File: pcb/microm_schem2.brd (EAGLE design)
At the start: 101.6 x 81.3 mm, 77 parts, among them Q1 16 MHz

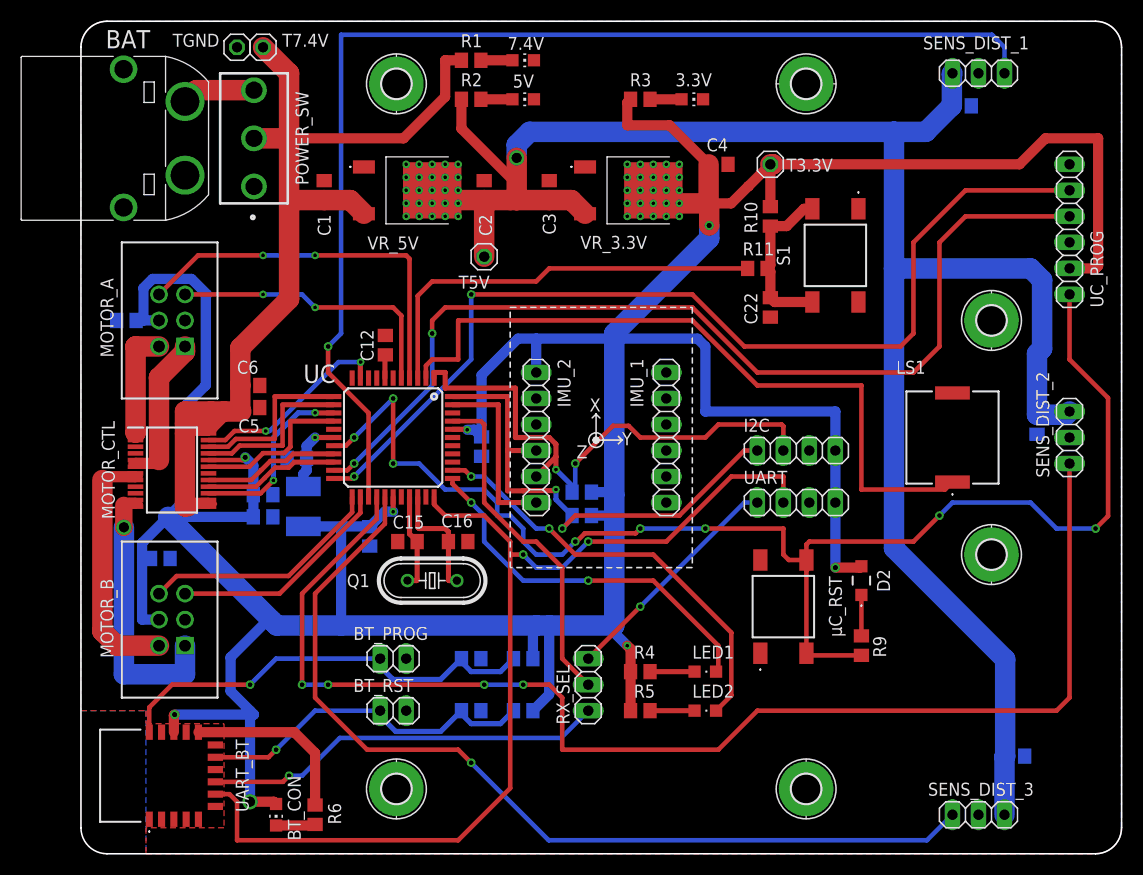
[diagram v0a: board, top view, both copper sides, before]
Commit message: Optimizations on pcb, unify via sizes and trace widths.
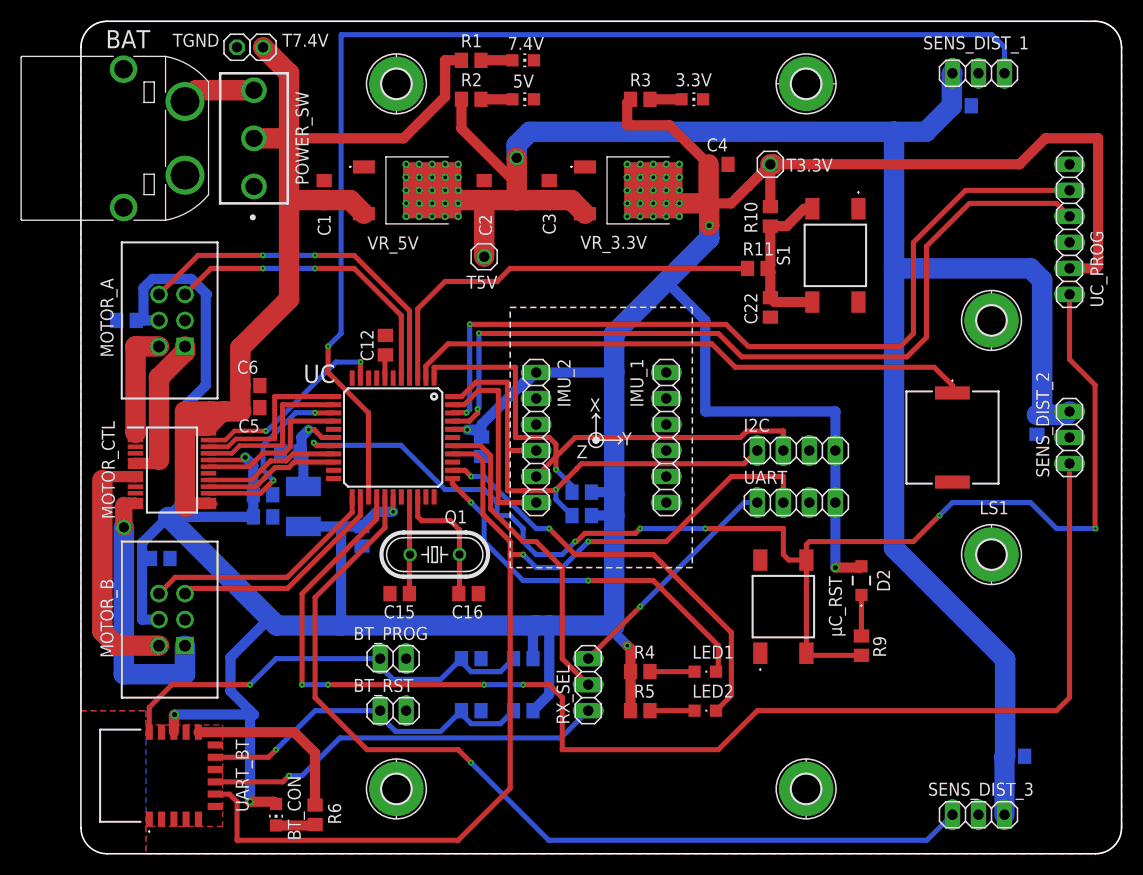
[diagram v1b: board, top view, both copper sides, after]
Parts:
- moved C16 5.18 mm to (37.8, 25.4)
- moved C15 5.14 mm to (31.1, 25.4)
- moved Q1 2.55 mm to (34.5, 29.2)
- moved C11 0.90 mm to (20.4, 39.2)
- moved C10 0.76 mm to (27.4, 31.0)
- turned LS1 to 270 degrees
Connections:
- removed net PG_EC1: UC.22, UC_PROG.5
- removed net PG_ED1: UC.21, UC_PROG.4
- new net PG_EC3: UC.42, UC_PROG.5
- new net PG_ED3: UC.41, UC_PROG.4
- net UART_RX: now also UC.38; no longer UC.41
- net UART_TX: now also UC.37; no longer UC.33
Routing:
- net PG_ED1: track 97.0 -> 0.00 mm, vias 2 -> 0
- net PG_EC1: track 96.6 -> 0.00 mm, vias 2 -> 0
- net PG_ED3: track 0.00 -> 81.1 mm, vias 0 -> 2
- net PG_EC3: track 0.00 -> 81.1 mm, vias 0 -> 2
- net BUZZ_PWM: track 69.8 -> 55.9 mm
- net +3V3: track 396.8 -> 388.0 mm
- net MCLR: track 134.7 -> 130.3 mm, vias 8 -> 6
- net MA_ENC_A: track 37.8 -> 34.8 mm
- net UART_TX: track 102.1 -> 104.7 mm
- net UART_RX: track 33.6 -> 31.2 mm
- net MA_ENC_B: track 28.1 -> 30.2 mm
- net IMU_INT: track 17.7 -> 19.7 mm
- net N$5: track 7.07 -> 8.79 mm
- net I2C_SDA: track 55.3 -> 53.8 mm, vias 2 -> 1
- net OSC2: track 11.7 -> 12.8 mm
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
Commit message: More wiring optimizations.
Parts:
- added C23: 100nF, rcl:C0805
- added LED3, LED4: red, 2mA, 2.1V, led:CHIPLED_0805
- added R14, R15: 680Ω, rcl:R0805
- C12: value 10uF, 10-20V, low-esr -> opt
- C13: value 100nF, 10-20V, low-esr -> 10uF, 10-20V, low-esr
- C15: value 20pF, low-esr, ceramic -> 100nF, 10-20V, low-esr
- C17: value 10 uF -> 20pF, low-esr, ceramic
- C20: value 1uF -> 10 uF
- C22: value 100nF -> 1uF
- moved C17 69.1 mm to (35.9, 25.4), flipped to the top
- moved C22 53.6 mm to (26.2, 18.9), flipped to the bottom, turned to 90 degrees
- moved C20 53.3 mm to (91.2, 9.53)
- moved C19 32.5 mm to (93.3, 41.9), turned to 270 degrees
- moved C18 32.0 mm to (86.0, 73.0), turned to 180 degrees
- moved C13 25.4 mm to (29.7, 49.7), flipped to the top, turned to 270 degrees
- moved C15 23.6 mm to (7.75, 28.8), flipped to the bottom
- moved C14 23.5 mm to (4.45, 52.1), turned to 0 degrees
- moved C12 15.5 mm to (20.4, 37.2), flipped to the bottom, turned to 180 degrees
- moved R13 14.9 mm to (28.3, 14.4), turned to 90 degrees
- moved R12 14.9 mm to (28.3, 18.9), turned to 90 degrees
- moved C21 12.8 mm to (26.2, 14.4), turned to 90 degrees
- moved R11 10.9 mm to (76.2, 53.3), turned to 270 degrees
- moved R10 8.98 mm to (76.2, 63.5)
- moved BT_PROG 8.89 mm to (21.6, 18.9)
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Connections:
- new net LED3: LED3.C, UC.35
- new net LED4: LED4.C, UC.36
- new net N$61: LED3.A, R14.2
- new net N$62: LED4.A, R15.2
- net +3V3: now also C15.1, R14.1, R15.1; no longer C13.1
- net +5V: now also C20.1; no longer C17.1
- net BT_PROG: now also C22.1; no longer C21.1
- net BT_RESET: now also C21.1; no longer C20.1
- net GND: now also C13.1, C23.2; no longer C13.2
- net LED1: now also UC.33; no longer UC.34
- net LED2: now also UC.34; no longer UC.35
- net MB_ENC_A: now also UC.22; no longer UC.24
- net MB_ENC_B: now also UC.21; no longer UC.23
- net N$5: now also C12.2
- net N$6: now also C23.1; no longer C22.1
- net OSC1: now also C16.1; no longer C15.1
- net OSC2: now also C17.1; no longer C16.1
- net SENS_DIST_1: now also UC.24; no longer UC.25
- net SENS_DIST_2: now also UC.25; no longer UC.26
- net SENS_DIST_3: now also UC.23; no longer UC.27
- net UART_RX: now also UC.37; no longer UC.38
- net UART_TX: now also UC.38; no longer UC.37
- net VCAP/VDDCORE: now also C13.2; no longer C12.2
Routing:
- net LED4: track 0.00 -> 50.3 mm, vias 0 -> 2
- net LED3: track 0.00 -> 45.3 mm, vias 0 -> 2
- net SENS_DIST_1: track 115.1 -> 158.2 mm, vias 1 -> 2
- net +3V3: track 388.0 -> 364.5 mm, vias 8 -> 9
- net SENS_DIST_2: track 126.8 -> 111.1 mm, vias 4 -> 2
- net BT_PROG: track 43.5 -> 28.0 mm
- net BT_RESET: track 34.5 -> 19.0 mm
- net UART_DBG_RX: track 22.8 -> 33.2 mm, vias 1 -> 0
- net BUTTON1: track 40.6 -> 49.9 mm
- net SENS_DIST_3: track 91.5 -> 83.1 mm, vias 1 -> 2
- net UART_BT_RX: track 39.3 -> 44.7 mm, vias 1 -> 0
- net N$6: track 16.3 -> 21.7 mm
- net BT_STATUS: track 17.3 -> 12.3 mm
- net UART_TX: track 104.7 -> 109.0 mm, vias 2 -> 0
- net N$62: track 0.00 -> 4.22 mm
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
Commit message: Few more optimizations.
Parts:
- R10, R9: value 10kΩ -> 2.2kΩ
- R11: value 1kΩ -> 10kΩ
- R13: value 10kΩ -> 1kΩ
- R14, R15: value 680Ω -> 10kΩ
- R6: value 180Ω -> 680Ω
- R7: value 2.2kΩ -> 680Ω
- R8: value 2.2kΩ -> 180Ω
- moved R12 65.4 mm to (76.2, 63.5), flipped to the top
- moved R13 61.7 mm to (76.2, 53.3), flipped to the top, turned to 270 degrees
- moved R8 44.8 mm to (17.8, 6.35), flipped to the top, turned to 270 degrees
- moved R10 36.9 mm to (49.0, 38.5), flipped to the bottom, turned to 0 degrees
- moved R6 36.6 mm to (53.3, 14.9), turned to 0 degrees
- moved R11 34.3 mm to (76.1, 19.1), turned to 90 degrees
- moved R9 32.2 mm to (49.0, 36.4), flipped to the bottom, turned to 0 degrees
- moved R14 25.3 mm to (28.3, 18.9), flipped to the bottom, turned to 90 degrees
- moved R15 25.1 mm to (28.3, 14.4), flipped to the bottom, turned to 90 degrees
- moved R7 24.1 mm to (53.3, 12.7), flipped to the top
- moved C13 1.94 mm to (27.8, 50.0), turned to 0 degrees
- moved C9 0.63 mm to (39.8, 39.8)
- moved C16 0.38 mm to (31.5, 25.4)
- moved C17 0.25 mm to (35.7, 25.4)
- moved C11 0.25 mm to (20.2, 39.2)
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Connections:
- removed net UART_BT_RX_IND: UART_BT.6
- net +3V3: now also R10.1, R14.2, R15.2, R6.1, R9.1; no longer R10.2, R13.2, R14.1, R15.1, R8.1
- net BT_PROG: now also R14.1; no longer R12.1
- net BT_RESET: now also R15.1; no longer R13.1
- net BT_STATUS: now also R8.1; no longer R6.1
- net BUTTON1: now also R13.2; no longer R11.2
- net I2C_SCL: now also R9.2; no longer R7.2
- net I2C_SDA: now also R10.2; no longer R8.2
- net MCLR: now also R11.1; no longer R9.1
- net N$1: now also R8.2; no longer R6.2
- net N$6: now also R12.1, R13.1; no longer R10.1, R11.1
- net N$61: now also R6.2; no longer R14.2
- net N$62: now also R7.2; no longer R15.2
- net N$7: now also R11.2; no longer R9.2
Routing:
- net GND: track 0.00 -> 14.6 mm, vias 0 -> 4
- net +3V3: track 364.5 -> 366.6 mm
- net SENS_DIST_3: track 83.1 -> 85.0 mm
- net VCAP/VDDCORE: track 2.28 -> 3.98 mm
- net SENS_DIST_1: track 158.2 -> 159.7 mm
- net SENS_DIST_2: track 111.1 -> 112.3 mm
- net LED1: track 36.1 -> 37.0 mm
- net MCLR: track 132.4 -> 133.1 mm

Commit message: Fix DRC issues.
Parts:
- moved T7.4V 0.63 mm to (17.8, 78.1)
- moved TGND 0.63 mm to (15.2, 78.1)
- moved C7 0.25 mm to (16.8, 35.1), turned to 0 degrees
- moved C8 0.25 mm to (16.8, 32.9), turned to 0 degrees
- moved R4 0.25 mm to (53.6, 19.2)
- moved R5 0.25 mm to (53.6, 17.0)
- moved R6 0.25 mm to (53.6, 14.9)
- moved R7 0.25 mm to (53.6, 12.7)
- moved R8 0.25 mm to (18.0, 6.35)
- moved C16 0.13 mm to (31.4, 25.4)
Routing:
- net GND: track 14.6 -> 32.8 mm, vias 4 -> 10
- net MB_OUT1: track 29.9 -> 25.5 mm
- net +7V4: track 104.2 -> 102.4 mm
- net MA_OUT1: track 11.9 -> 10.1 mm
- net MB_ENC_A: track 19.2 -> 20.2 mm
- net BUTTON1: track 49.9 -> 48.9 mm
- net N$6: track 21.7 -> 20.8 mm
- net LED1: track 37.0 -> 36.2 mm
- net MCLR: track 133.1 -> 132.5 mm
- net +3V3: track 366.6 -> 367.2 mm
- net MA_OUT2: track 20.3 -> 19.7 mm
- net I2C_SDA: track 51.6 -> 51.0 mm
- net SENS_DIST_2: track 112.3 -> 112.8 mm
- net UART_TX: track 109.0 -> 108.5 mm
